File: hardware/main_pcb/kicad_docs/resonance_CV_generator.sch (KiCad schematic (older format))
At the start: 11 parts, among them U5 TL072

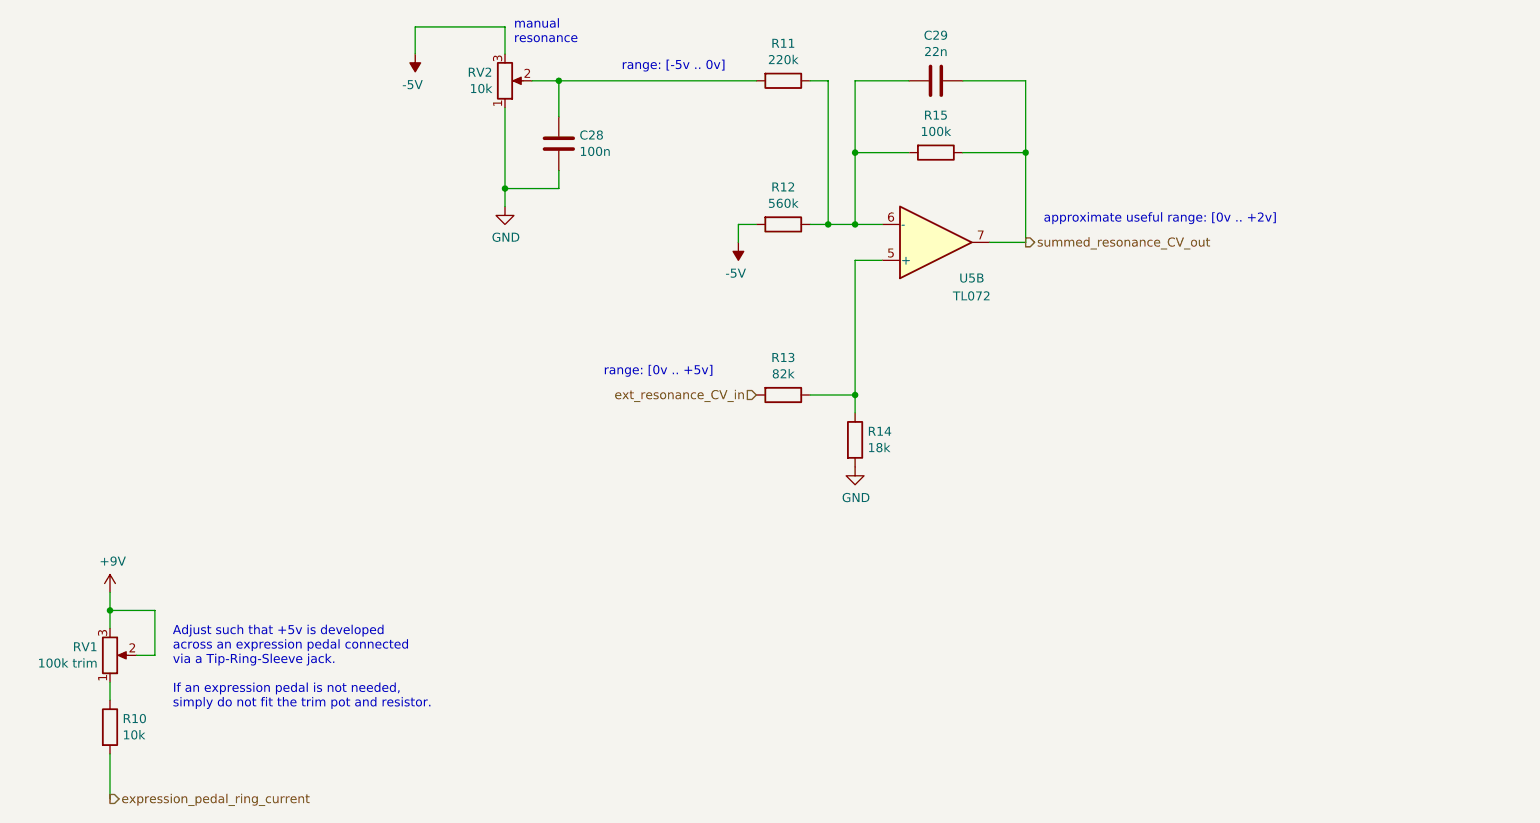
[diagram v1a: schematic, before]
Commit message: center envelope follower around +1v, tidy up
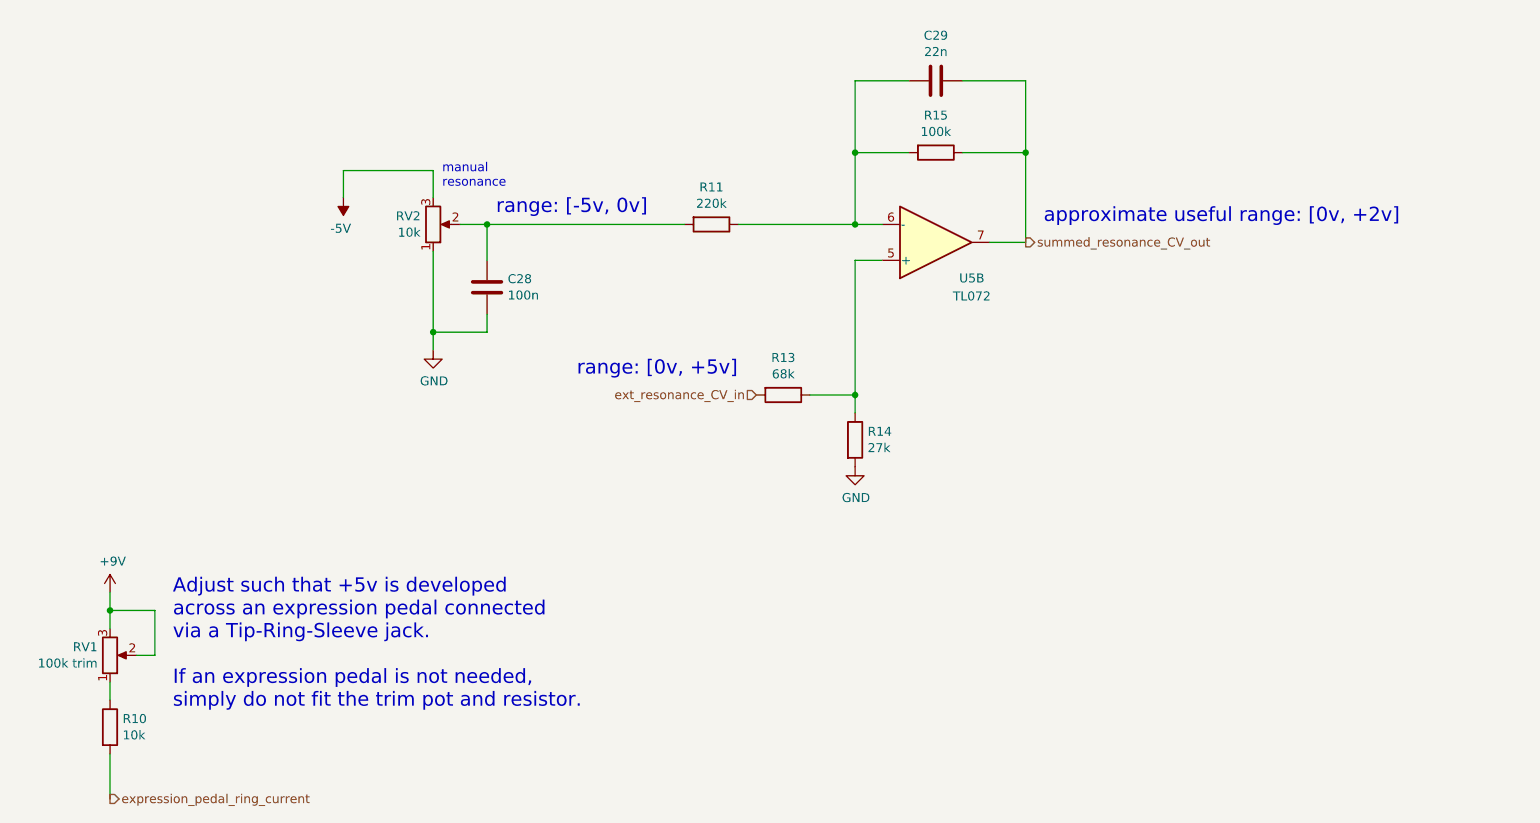
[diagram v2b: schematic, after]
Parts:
- removed R12: 560k, Resistor_SMD:R_0805_2012Metric, symbol Device:R
- R13: value 82k -> 68k
- R14: value 18k -> 27k
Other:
- note added: "approximate useful range: [0v, +2v]"
- note added: "range: [-5v, 0v]"
- note added: "range: [0v, +5v]"
- note removed: "approximate useful range: [0v .. +2v]"
- note removed: "range: [-5v .. 0v]"
- note removed: "range: [0v .. +5v]"
- moved on the sheet: C28, R11, RV2
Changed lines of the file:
@@
 Sheet 7 8
 Title "Whooshy Sound Filter Pedal"
-Date "2021-06-29"
-Rev "0"
+Date "2021-08-05"
+Rev "0.1"
 Comp ""
 Comment1 "creativecommons.org/licenses/by/4.0/"
@@
 P 5700 4950
 F 0 "R14" H 5770 4996 50  0000 L CNN
-F 1 "18k" H 5770 4905 50  0000 L CNN
+F 1 "27k" H 5770 4905 50  0000 L CNN
 F 2 "Resistor_SMD:R_0805_2012Metric" V 5630 4950 50  0001 C CNN
 F 3 "~" H 5700 4950 50  0001 C CNN
@@
 L Device:R R11
 U 1 1 60F682DF
-P 5300 2950
-F 0 "R11" V 5093 2950 50  0000 C CNN
-F 1 "220k" V 5184 2950 50  0000 C CNN
-F 2 "Resistor_SMD:R_0805_2012Metric" V 5230 2950 50  0001 C CNN
-F 3 "~" H 5300 2950 50  0001 C CNN
-	1    5300 2950
+P 4900 3750
+F 0 "R11" V 4693 3750 50  0000 C CNN
+F 1 "220k" V 4784 3750 50  0000 C CNN
+F 2 "Resistor_SMD:R_0805_2012Metric" V 4830 3750 50  0001 C CNN
+F 3 "~" H 4900 3750 50  0001 C CNN
+	1    4900 3750
 	0    1    1    0
 $EndComp
@@
 L Device:R_POT RV2
 U 1 1 60F6D28A
-P 3750 2950
-F 0 "RV2" H 3680 2904 50  0000 R CNN
-F 1 "10k" H 3680 2995 50  0000 R CNN
-F 2 "Potentiometer_THT:Potentiometer_Alpha_RD901F-40-00D_Single_Vertical" H 3750 2950 50  0001 C CNN
-F 3 "~" H 3750 2950 50  0001 C CNN
-	1    3750 2950
+P 3350 3750
+F 0 "RV2" H 3280 3704 50  0000 R CNN
+F 1 "10k" H 3280 3795 50  0000 R CNN
+F 2 "Potentiometer_THT:Potentiometer_Alpha_RD901F-40-00D_Single_Vertical" H 3350 3750 50  0001 C CNN
+F 3 "~" H 3350 3750 50  0001 C CNN
+	1    3350 3750
 	1    0    0    1
 $EndComp
@@
 P 5300 4700
 F 0 "R13" V 5093 4700 50  0000 C CNN
-F 1 "82k" V 5184 4700 50  0000 C CNN
+F 1 "68k" V 5184 4700 50  0000 C CNN
 F 2 "Resistor_SMD:R_0805_2012Metric" V 5230 4700 50  0001 C CNN
 F 3 "~" H 5300 4700 50  0001 C CNN
@@
 L power:GND #PWR037
 U 1 1 60F73B74
-P 3750 3650
-F 0 "#PWR037" H 3750 3400 50  0001 C CNN
-F 1 "GND" H 3755 3477 50  0000 C CNN
-F 2 "" H 3750 3650 50  0001 C CNN
-F 3 "" H 3750 3650 50  0001 C CNN
-	1    3750 3650
+P 3350 4450
+F 0 "#PWR037" H 3350 4200 50  0001 C CNN
+F 1 "GND" H 3355 4277 50  0000 C CNN
+F 2 "" H 3350 4450 50  0001 C CNN
+F 3 "" H 3350 4450 50  0001 C CNN
+	1    3350 4450
 	1    0    0    -1
 $EndComp
@@
 $EndComp
 Wire Wire Line
-	3250 2800 3250 2650
-Wire Wire Line
-	3250 2650 3750 2650
-Wire Wire Line
-	3750 2650 3750 2800
-Wire Wire Line
-	3900 2950 4050 2950
+	2850 3600 2850 3450
+Wire Wire Line
+	2850 3450 3350 3450
+Wire Wire Line
+	3350 3450 3350 3600
+Wire Wire Line
+	3500 3750 3650 3750
 Wire Wire Line
 	6000 3350 5700 3350
@@
 L Device:C C28
 U 1 1 60F8C8BB
-P 4050 3300
-F 0 "C28" H 4165 3346 50  0000 L CNN
-F 1 "100n" H 4165 3255 50  0000 L CNN
-F 2 "Capacitor_SMD:C_0805_2012Metric" H 4088 3150 50  0001 C CNN
-F 3 "~" H 4050 3300 50  0001 C CNN
-	1    4050 3300
-	1    0    0    -1
-$EndComp
-Wire Wire Line
-	3750 3100 3750 3550
-Wire Wire Line
-	4050 3450 4050 3550
-Wire Wire Line
-	4050 3550 3750 3550
-Connection ~ 3750 3550
-Wire Wire Line
-	3750 3550 3750 3650
-Wire Wire Line
-	4050 3150 4050 2950
-Connection ~ 4050 2950
-Wire Wire Line
-	4050 2950 5150 2950
-$Comp
-L Device:R R12
-U 1 1 6102ECB0
-P 5300 3750
-F 0 "R12" V 5093 3750 50  0000 C CNN
-F 1 "560k" V 5184 3750 50  0000 C CNN
-F 2 "Resistor_SMD:R_0805_2012Metric" V 5230 3750 50  0001 C CNN
-F 3 "~" H 5300 3750 50  0001 C CNN
-	1    5300 3750
-	0    1    1    0
-$EndComp
-Wire Wire Line
-	5450 3750 5550 3750
+P 3650 4100
+F 0 "C28" H 3765 4146 50  0000 L CNN
+F 1 "100n" H 3765 4055 50  0000 L CNN
+F 2 "Capacitor_SMD:C_0805_2012Metric" H 3688 3950 50  0001 C CNN
+F 3 "~" H 3650 4100 50  0001 C CNN
+	1    3650 4100
+	1    0    0    -1
+$EndComp
+Wire Wire Line
+	3350 3900 3350 4350
+Wire Wire Line
+	3650 4250 3650 4350
+Wire Wire Line
+	3650 4350 3350 4350
+Connection ~ 3350 4350
+Wire Wire Line
+	3350 4350 3350 4450
+Wire Wire Line
+	3650 3950 3650 3750
+Connection ~ 3650 3750
+Wire Wire Line
+	3650 3750 4750 3750
 Connection ~ 5700 3750
-Wire Wire Line
-	5550 3750 5550 2950
-Wire Wire Line
-	5450 2950 5550 2950
-Connection ~ 5550 3750
-Wire Wire Line
-	5550 3750 5700 3750
-Wire Wire Line
-	5050 3850 5050 3750
-Wire Wire Line
-	5050 3750 5150 3750
-Text Notes 6750 3750 0    50   ~ 0
-approximate useful range: [0v .. +2v]
-Text Notes 4400 2900 0    50   ~ 0
-range: [-5v .. 0v]
-Text Notes 4300 4600 0    50   ~ 0
-range: [0v .. +5v]
+Text Notes 6750 3750 0    79   ~ 0
+approximate useful range: [0v, +2v]
+Text Notes 3700 3700 0    79   ~ 0
+range: [-5v, 0v]
+Text Notes 4150 4600 0    79   ~ 0
+range: [0v, +5v]
 $Comp
 L power:-5V #PWR036
 U 1 1 6126C044
-P 3250 2800
-F 0 "#PWR036" H 3250 2900 50  0001 C CNN
-F 1 "-5V" H 3265 2973 50  0000 C CNN
-F 2 "" H 3250 2800 50  0001 C CNN
-F 3 "" H 3250 2800 50  0001 C CNN
-	1    3250 2800
-	-1   0    0    1
-$EndComp
-$Comp
-L power:-5V #PWR038
-U 1 1 6126BC27
-P 5050 3850
-F 0 "#PWR038" H 5050 3950 50  0001 C CNN
-F 1 "-5V" H 5065 4023 50  0000 C CNN
-F 2 "" H 5050 3850 50  0001 C CNN
-F 3 "" H 5050 3850 50  0001 C CNN
-	1    5050 3850
+P 2850 3600
+F 0 "#PWR036" H 2850 3700 50  0001 C CNN
+F 1 "-5V" H 2865 3773 50  0000 C CNN
+F 2 "" H 2850 3600 50  0001 C CNN
+F 3 "" H 2850 3600 50  0001 C CNN
+	1    2850 3600
 	-1   0    0    1
 $EndComp
@@
 Wire Wire Line
 	1550 6950 1550 6700
-Text Notes 1900 6450 0    50   ~ 0
+Text Notes 1900 6450 0    79   ~ 0
 Adjust such that +5v is developed\nacross an expression pedal connected\nvia a Tip-Ring-Sleeve jack.\n\nIf an expression pedal is not needed, \nsimply do not fit the trim pot and resistor.
-Text Notes 3800 2750 0    50   ~ 0
+Text Notes 3400 3550 0    50   ~ 0
 manual\nresonance
+Wire Wire Line
+	5050 3750 5700 3750
 $EndSCHEMATC
